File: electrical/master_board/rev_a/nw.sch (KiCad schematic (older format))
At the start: 0 parts

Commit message: Updated some of the schematics and PCB's via hr2_models.py .
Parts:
- added CN70: HCSR04H;F1X4, HR2:HCSR04_F1x4H_MATE, symbol HR2:HCSR04H;F1X4
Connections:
- no-connect marks 0 -> 4
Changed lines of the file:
@@
 Comment4 ""
 $EndDescr
+$Comp
+L HR2:HCSR04H;F1X4 CN70
+U 1 1 5EE6C4D8
+P 4550 3550
+F 0 "CN70" H 4900 3700 50  0000 C CNN
+F 1 "HCSR04H;F1X4" H 4900 3100 50  0000 C CNN
+F 2 "HR2:HCSR04_F1x4H_MATE" H 4750 3600 60  0001 L CNN
+F 3 "https://cdn.sparkfun.com/datasheets/Sensors/Proximity/HCSR04.pdf" H 4750 3400 60  0001 L CNN
+F 4 "https://cdn.sparkfun.com/datasheets/Sensors/Proximity/HCSR04.pdf" H 4750 3500 60  0001 L CNN "manf#"
+F 5 "HC-SR04 Sonar (High Profile Receptacle)" H 4750 3300 60  0001 L CNN "Field5"
+	1    4550 3550
+	1    0    0    -1
+$EndComp
+NoConn ~ 5250 3550
+NoConn ~ 5250 3650
+NoConn ~ 5250 3750
+NoConn ~ 5250 3850
 $EndSCHEMATC

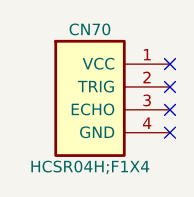
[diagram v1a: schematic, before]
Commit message: The PCBChunk'ification of Sonars is complete.
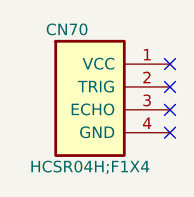
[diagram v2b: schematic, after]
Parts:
- CN70: footprint HR2:HCSR04_F1x4H_MATE -> HR2:HCSR04_F1x4H
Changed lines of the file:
@@
 Comment4 ""
 $EndDescr
+NoConn ~ 5250 3550
+NoConn ~ 5250 3650
+NoConn ~ 5250 3750
+NoConn ~ 5250 3850
 $Comp
 L HR2:HCSR04H;F1X4 CN70
-U 1 1 5EE6C4D8
+U 1 1 5F0B8A7B
 P 4550 3550
-F 0 "CN70" H 4900 3700 50  0000 C CNN
+F 0 "CN70" H 4800 3700 50  0000 C CNN
 F 1 "HCSR04H;F1X4" H 4900 3100 50  0000 C CNN
-F 2 "HR2:HCSR04_F1x4H_MATE" H 4750 3600 60  0001 L CNN
+F 2 "HR2:HCSR04_F1x4H" H 4750 3600 60  0001 L CNN
 F 3 "https://cdn.sparkfun.com/datasheets/Sensors/Proximity/HCSR04.pdf" H 4750 3400 60  0001 L CNN
 F 4 "https://cdn.sparkfun.com/datasheets/Sensors/Proximity/HCSR04.pdf" H 4750 3500 60  0001 L CNN "manf#"
@@
 	1    0    0    -1
 $EndComp
-NoConn ~ 5250 3550
-NoConn ~ 5250 3650
-NoConn ~ 5250 3750
-NoConn ~ 5250 3850
 $EndSCHEMATC

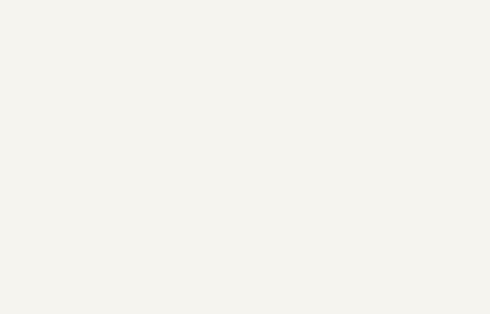
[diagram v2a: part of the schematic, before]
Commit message: Added spacer mounting holes to schematics and associated PCB's.
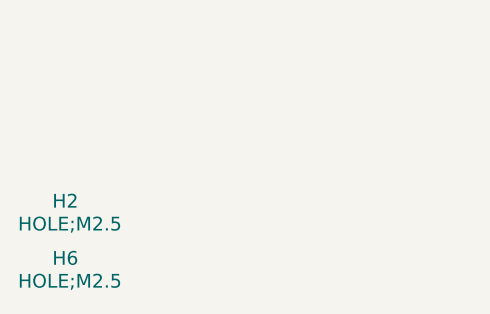
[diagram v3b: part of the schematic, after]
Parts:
- added H2, H6: HOLE;M2.5, MountingHole:MountingHole_2.7mm_M2.5, symbol HR2:HOLE;M2.5
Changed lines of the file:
@@
+	1    0    0    -1
+$EndComp
+$Comp
+L HR2:HOLE;M2.5 H6
+U 1 1 5F2F7B9C
+P 2100 4450
+F 0 "H6" H 2050 4500 60  0000 L CNN
+F 1 "HOLE;M2.5" H 1900 4400 60  0000 L CNN
+F 2 "MountingHole:MountingHole_2.7mm_M2.5" H 2300 4500 60  0001 L CNN
+F 3 "M2.5 Mounting Hole" H 2300 4300 60  0001 L CNN
+	1    2100 4450
+	1    0    0    -1
+$EndComp
+$Comp
+L HR2:HOLE;M2.5 H2
+U 1 1 5F2F8125
+P 2100 4200
+F 0 "H2" H 2050 4250 60  0000 L CNN
+F 1 "HOLE;M2.5" H 1900 4150 60  0000 L CNN
+F 2 "MountingHole:MountingHole_2.7mm_M2.5" H 2300 4250 60  0001 L CNN
+F 3 "M2.5 Mounting Hole" H 2300 4050 60  0001 L CNN
+	1    2100 4200
 	1    0    0    -1
 $EndComp

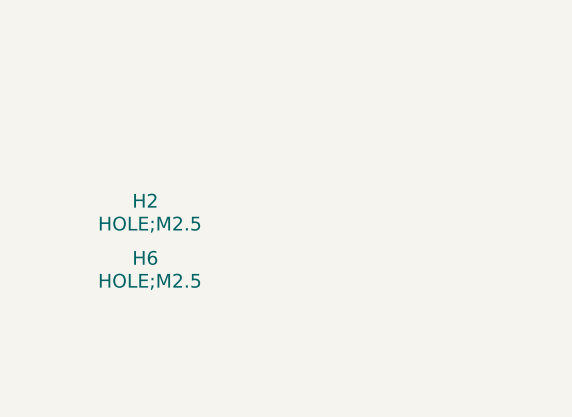
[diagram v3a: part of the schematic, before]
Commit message: Placed all of the Groves on the PCB's.
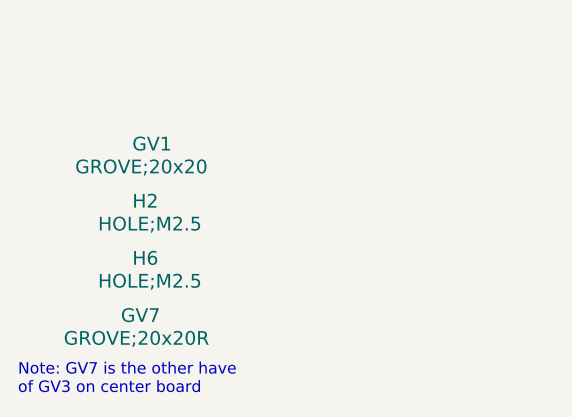
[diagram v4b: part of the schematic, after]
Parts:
- added GV1: GROVE;20x20, HR2:GROVE20x20, symbol HR2:GROVE;20x20
- added GV7: GROVE;20x20R, HR2:GROVE20x20R, symbol HR2:GROVE;20x20R
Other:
- note added: "Note: GV7 is the other have\nof GV3 on center board"
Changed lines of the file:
@@
 	1    0    0    -1
 $EndComp
+$Comp
+L HR2:GROVE;20x20 GV1
+U 1 1 5F2F999C
+P 2100 3950
+F 0 "GV1" H 2050 4000 60  0000 L CNN
+F 1 "GROVE;20x20" H 1800 3900 60  0000 L CNN
+F 2 "HR2:GROVE20x20" H 2300 4000 60  0001 L CNN
+F 3 "Grove 20x20 Module" H 2300 3800 60  0001 L CNN
+F 4 "Grove 20x20 Module" H 2300 3900 60  0001 L CNN "manf#"
+	1    2100 3950
+	1    0    0    -1
+$EndComp
+$Comp
+L HR2:GROVE;20x20R GV7
+U 1 1 5F303BB1
+P 2100 4700
+F 0 "GV7" H 2000 4750 60  0000 L CNN
+F 1 "GROVE;20x20R" H 1750 4650 60  0000 L CNN
+F 2 "HR2:GROVE20x20R" H 2300 4750 60  0001 L CNN
+F 3 "Grove 20x20 Module" H 2300 4550 60  0001 L CNN
+F 4 "Grove 20x20 Module" H 2300 4650 60  0001 L CNN "manf#"
+	1    2100 4700
+	1    0    0    -1
+$EndComp
+Text Notes 1550 5000 0    50   ~ 0
+Note: GV7 is the other have\nof GV3 on center board
 $EndSCHEMATC

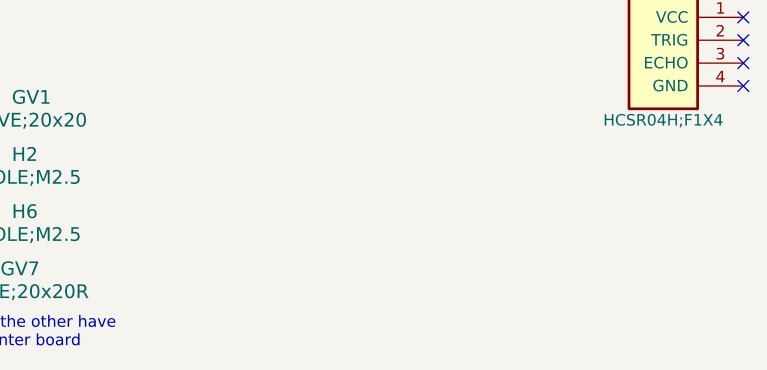
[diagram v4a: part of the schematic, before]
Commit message: Added LED's to the PCB's.
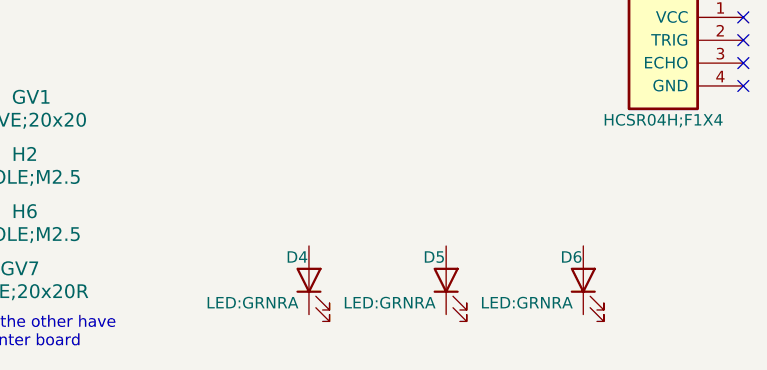
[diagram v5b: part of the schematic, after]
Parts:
- added D4, D5, D6: LED:GRNRA, HR2:LED_GRNRA, symbol Device:LED
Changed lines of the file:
@@
 Text Notes 1550 5000 0    50   ~ 0
 Note: GV7 is the other have\nof GV3 on center board
+$Comp
+L Device:LED D4
+U 1 1 5F30BC5B
+P 3350 4700
+F 0 "D4" V 3450 4800 50  0000 R CNN
+F 1 "LED:GRNRA" V 3250 5150 50  0000 R CNN
+F 2 "HR2:LED_GRNRA" H 3350 4700 50  0001 C CNN
+F 3 "~" H 3350 4700 50  0001 C CNN
+	1    3350 4700
+	0    -1   -1   0
+$EndComp
+$Comp
+L Device:LED D5
+U 1 1 5F30DD43
+P 3950 4700
+F 0 "D5" V 4050 4800 50  0000 R CNN
+F 1 "LED:GRNRA" V 3850 5150 50  0000 R CNN
+F 2 "HR2:LED_GRNRA" H 3950 4700 50  0001 C CNN
+F 3 "~" H 3950 4700 50  0001 C CNN
+	1    3950 4700
+	0    -1   -1   0
+$EndComp
+$Comp
+L Device:LED D6
+U 1 1 5F30E439
+P 4550 4700
+F 0 "D6" V 4650 4800 50  0000 R CNN
+F 1 "LED:GRNRA" V 4450 5150 50  0000 R CNN
+F 2 "HR2:LED_GRNRA" H 4550 4700 50  0001 C CNN
+F 3 "~" H 4550 4700 50  0001 C CNN
+	1    4550 4700
+	0    -1   -1   0
+$EndComp
 $EndSCHEMATC

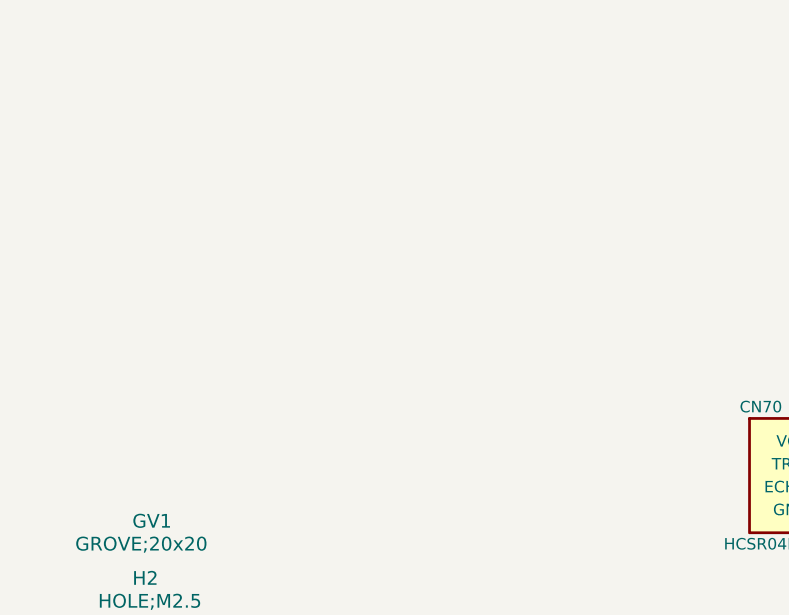
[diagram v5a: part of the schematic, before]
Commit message: Got Bridge connectors installed on PCB's. Tweaking still required.
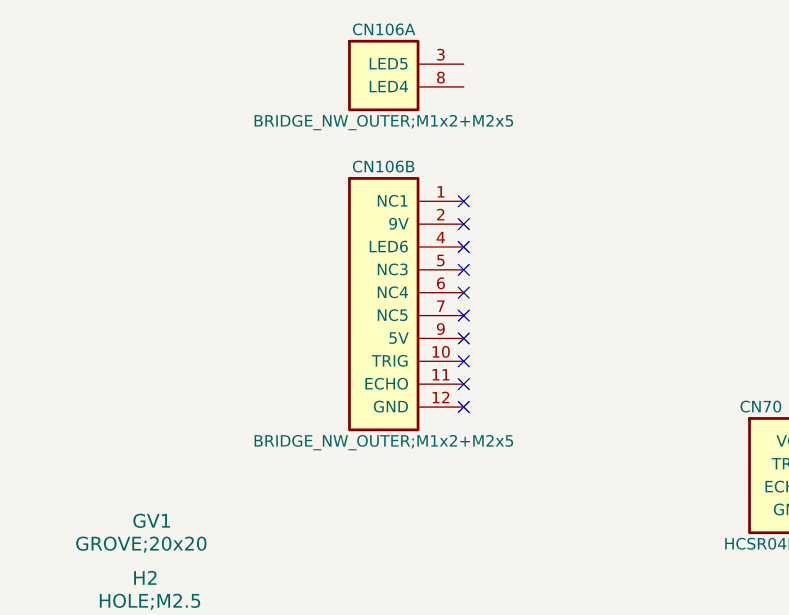
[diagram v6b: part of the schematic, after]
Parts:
- added CN106: BRIDGE_NW_OUTER;M1x2+M2x5, HR2:BRIDGE_NW_OUTER_M1x2+M2x5, symbol HR2:BRIDGE_NW_OUTER;M1x2+M2x5
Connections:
- no-connect marks 4 -> 14
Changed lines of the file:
@@
 	0    -1   -1   0
 $EndComp
+$Comp
+L HR2:BRIDGE_NW_OUTER;M1x2+M2x5 CN106
+U 1 1 5F3877C6
+P 2800 1900
+F 0 "CN106" H 3150 2050 50  0000 C CNN
+F 1 "BRIDGE_NW_OUTER;M1x2+M2x5" H 3150 1650 50  0000 C CNN
+F 2 "HR2:BRIDGE_NW_OUTER_M1x2+M2x5" H 3000 1950 60  0001 L CNN
+F 3 "" H 3000 1750 60  0001 L CNN
+F 4 "NW Outer Bridge Connectors" H 3000 1650 60  0001 L CNN "Field5"
+	1    2800 1900
+	1    0    0    -1
+$EndComp
+$Comp
+L HR2:BRIDGE_NW_OUTER;M1x2+M2x5 CN106
+U 2 1 5F389BE1
+P 2800 2500
+F 0 "CN106" H 3150 2650 50  0000 C CNN
+F 1 "BRIDGE_NW_OUTER;M1x2+M2x5" H 3150 1450 50  0000 C CNN
+F 2 "HR2:BRIDGE_NW_OUTER_M1x2+M2x5" H 3000 2550 60  0001 L CNN
+F 3 "" H 3000 2350 60  0001 L CNN
+F 4 "NW Outer Bridge Connectors" H 3000 2250 60  0001 L CNN "Field5"
+	2    2800 2500
+	1    0    0    -1
+$EndComp
+NoConn ~ 3500 2500
+NoConn ~ 3500 2600
+NoConn ~ 3500 2700
+NoConn ~ 3500 2800
+NoConn ~ 3500 2900
+NoConn ~ 3500 3000
+NoConn ~ 3500 3100
+NoConn ~ 3500 3200
+NoConn ~ 3500 3300
+NoConn ~ 3500 3400
 $EndSCHEMATC

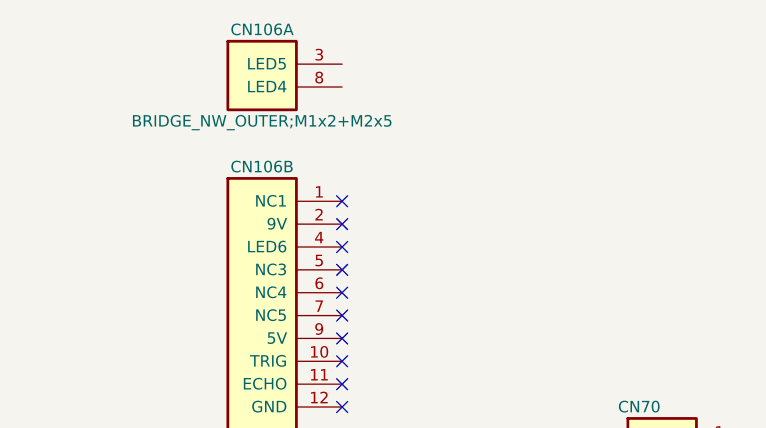
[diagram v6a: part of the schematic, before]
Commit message: The four corner boards ne/nw/se/sw are now zoned.
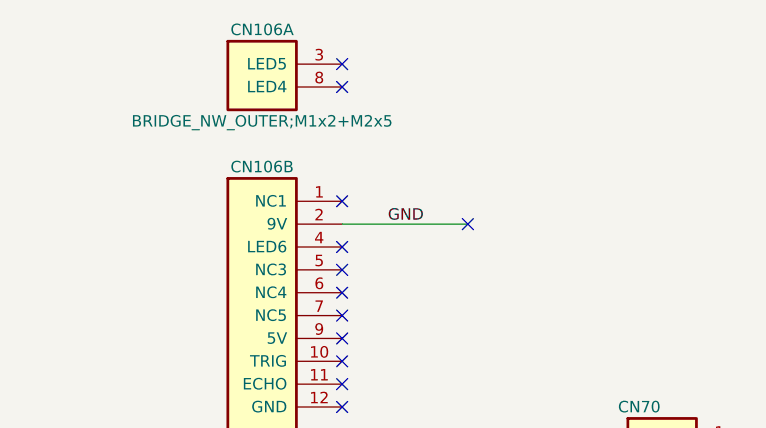
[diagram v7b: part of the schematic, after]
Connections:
- net GND: now reaches CN106.2 (9V)
- no-connect marks 14 -> 16
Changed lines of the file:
@@
 $EndComp
 NoConn ~ 3500 2500
-NoConn ~ 3500 2600
 NoConn ~ 3500 2700
 NoConn ~ 3500 2800
@@
 NoConn ~ 3500 3300
 NoConn ~ 3500 3400
+Wire Wire Line
+	3500 2600 4050 2600
+NoConn ~ 3500 1900
+NoConn ~ 3500 2000
+NoConn ~ 4050 2600
+Text Label 3700 2600 0    50   ~ 0
+GND
 $EndSCHEMATC

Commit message: Wrapped up NE PCB.
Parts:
- added Q4, Q5, Q6: 2N7000;SOT23, Package_TO_SOT_SMD:SOT-23, symbol Transistor_FET:2N7000
- added R10, R11, R12, R13, R14, R15, R16, R17, R18: 330Ω;1608, Resistor_SMD:R_0603_1608Metric, symbol Device:R_US
- D4, D5, D6: value LED:GRNRA -> LED;GRNRA
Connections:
- net GND: now also CN106.12 (GND), CN70.4 (GND), D4.1 (K), D5.1 (K), D6.1 (K); no longer CN106.2 (9V)
- net 5V: now reaches CN70.1 (VCC)
- net 5V: now also CN106.9 (5V)
- net TRIG: now reaches CN70.2 (TRIG)
- net TRIG: now also CN106.10 (TRIG)
- net ECHO: now reaches CN70.3 (ECHO)
- net ECHO: now also CN106.11 (ECHO)
- net at D4.2 (A): now also Q4.1 (S)
- net at D5.2 (A): now also Q5.1 (S)
- net at D6.2 (A): now also Q6.1 (S)
- net LED5: now reaches CN106.3 (LED5)
- net LED5: now also Q5.2 (G)
- net LED4: now reaches CN106.8 (LED4)
- net LED4: now also Q4.2 (G)
- net LED6: now reaches CN106.4 (LED6)
- net LED6: now also Q6.2 (G)
- new net: Q4.3 (D), R10.1, R11.1, R12.1
- new net: Q5.3 (D), R13.1, R14.1, R15.1
- new net: Q6.3 (D), R16.1, R17.1, R18.1
- new net 9V: CN106.2 (9V), R10.2, R11.2, R12.2, R13.2, R14.2, R15.2, R16.2, R17.2, R18.2
- no-connect marks 16 -> 5
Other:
- note added: "Note: GV7 is the other half of GV3 on center board"
- note removed: "Note: GV7 is the other have\nof GV3 on center board"
- moved on the sheet: CN106A, CN106B, CN70, D4, D5, D6
